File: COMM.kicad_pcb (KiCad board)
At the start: 4 copper layers, 90.2 x 95.9 mm, 41 parts, among them IC1 TLV61047DDCR, IC2 Voltage Converter (ADP7158ARD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, J1 SMA Conn. (RFPC-SMA30-F), U1 XBee Module (XBP9B-DMSTB002), U2 DMR Module (DMR818S-5W)

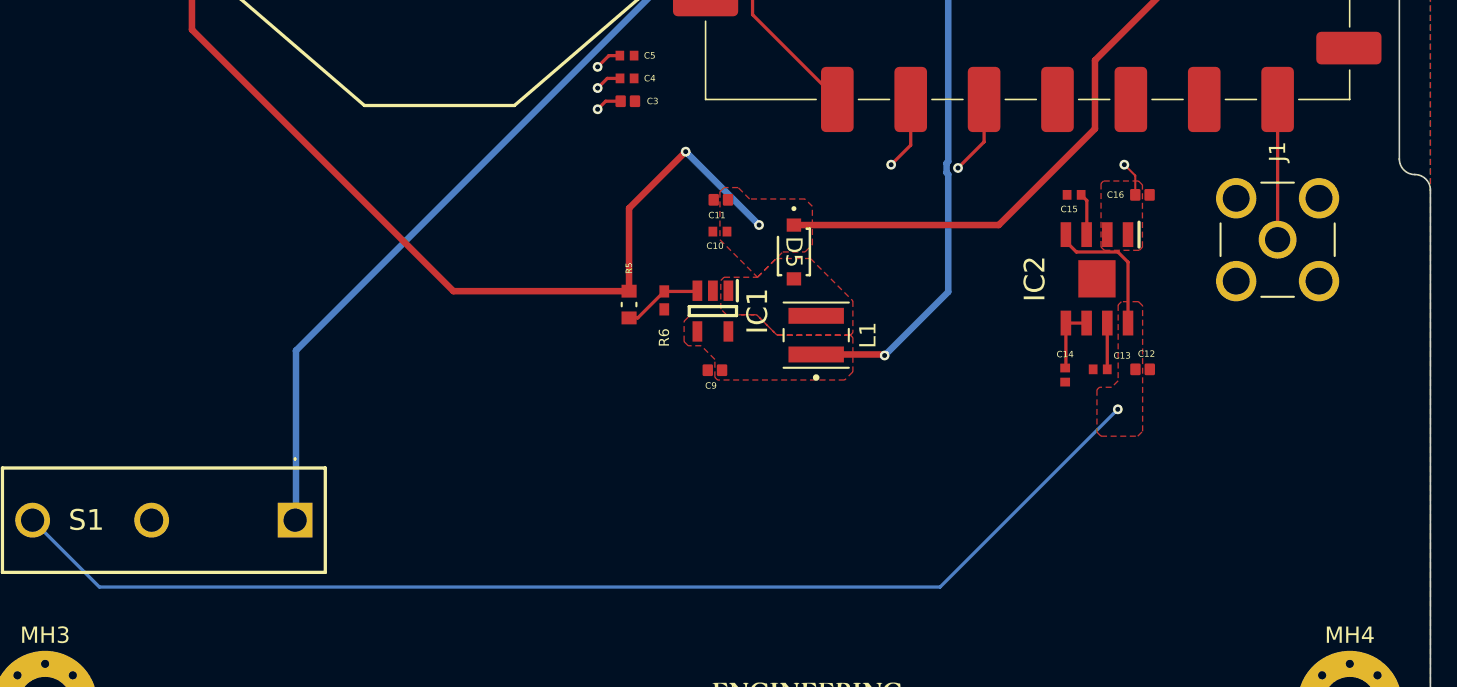
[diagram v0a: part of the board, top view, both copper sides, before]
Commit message: Switched positions for SMA connector and voltage regulator.
Signed-off-by: Logan Tolbert <xem6df@virginia.edu>
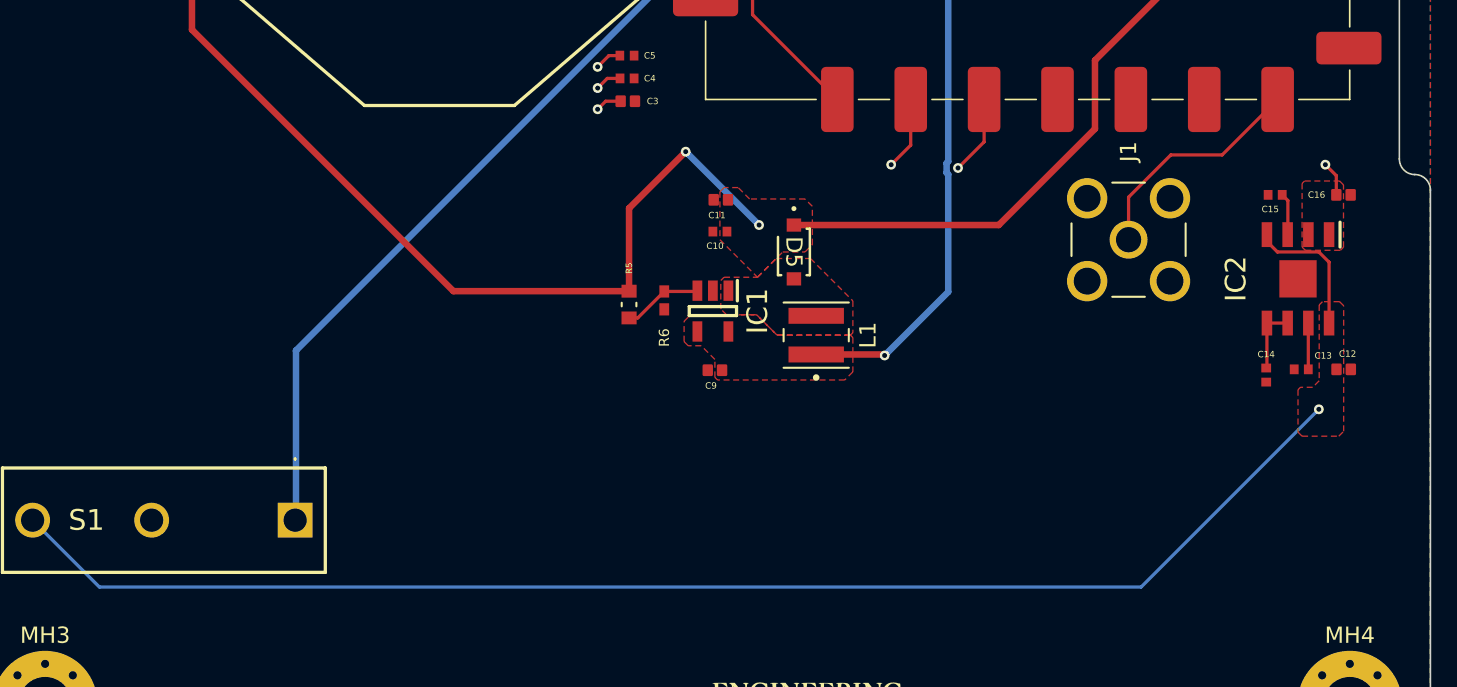
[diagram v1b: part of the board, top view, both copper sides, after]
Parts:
- moved C13 12.3 mm to (183.8, 123.3)
- moved C15 12.3 mm to (182.2, 112.7)
- moved IC2 12.3 mm to (183.7, 117.8)
- moved C12 12.3 mm to (186.4, 123.3)
- moved C14 12.3 mm to (181.7, 123.7)
- moved C16 12.3 mm to (186.4, 112.7)
- moved J1 9.14 mm to (173.3, 115.4)
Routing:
- net /Voltage Converter/VIN: track 81.3 -> 93.6 mm
- net /DMR818S 5W RF Module/ANT: track 8.60 -> 14.2 mm
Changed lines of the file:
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@@
 		(placed yes)
 		(layer "F.Cu")
-		(at 169.371 123.7 -90)
+		(at 181.7 123.7 -90)
 		(property "Reference" "C14"
 			(at -1.27 0 0)
@@
 	(footprint "RFPC-SMA30-F:GRADCONN_RFPC-SMA30-F"
 		(layer "F.Cu")
-		(at 182.4 115.4)
+		(at 173.26 115.4)
 		(property "Reference" "J1"
 			(at 0 -5.4 90)
@@
 		(placed yes)
 		(layer "F.Cu")
-		(at 171.321 117.8 -90)
+		(at 183.65 117.8 -90)
 		(descr "SOIC_N_EP")
 		(tags "Integrated Circuit")
@@
 	(footprint "C_10uF:CAPC1005X70N"
 		(layer "F.Cu")
-		(at 174.121 123.35)
+		(at 186.45 123.35)
 		(property "Reference" "C12"
 			(at 0.24 -0.95 0)
@@
 		(placed yes)
 		(layer "F.Cu")
-		(at 169.921 112.65 180)
+		(at 182.25 112.65 180)
 		(property "Reference" "C15"
 			(at 0.3 -0.88 0)
@@
 		(placed yes)
 		(layer "F.Cu")
-		(at 171.521 123.35 180)
+		(at 183.85 123.35 180)
 		(property "Reference" "C13"
 			(at -1.3462 0.8382 0)
@@
 		(placed yes)
 		(layer "F.Cu")
-		(at 174.11 112.65)
+		(at 186.439 112.65)
 		(property "Reference" "C16"
 			(at -1.651 0 0)
@@
 	)
 	(segment
-		(start 170.353 112.65)
-		(end 170.7 112.997)
+		(start 182.682 112.65)
+		(end 183.029 112.997)
 		(width 0.2)
 		(layer "F.Cu")
@@
 	)
 	(segment
-		(start 170.7 112.997)
-		(end 170.7 115.074)
+		(start 183.029 112.997)
+		(end 183.029 115.074)
 		(width 0.2)
 		(layer "F.Cu")
@@
 	)
 	(segment
-		(start 170.7 115.074)
-		(end 170.686 115.088)
+		(start 183.029 115.074)
+		(end 183.015 115.088)
 		(width 0.2)
 		(layer "F.Cu")
@@
 	)
 	(segment
-		(start 169.416 123.223)
-		(end 169.371 123.268)
+		(start 181.745 123.223)
+		(end 181.7 123.268)
 		(width 0.2)
 		(layer "F.Cu")
@@
 	)
 	(segment
-		(start 169.416 120.512)
-		(end 170.686 120.512)
+		(start 181.745 120.512)
+		(end 183.015 120.512)
 		(width 0.2)
 		(layer "F.Cu")
@@
 	)
 	(segment
-		(start 169.416 120.512)
-		(end 169.416 123.223)
+		(start 181.745 120.512)
+		(end 181.745 123.223)
 		(width 0.2)
 		(layer "F.Cu")
@@
 	)
 	(segment
-		(start 171.953 123.35)
-		(end 171.953 120.515)
+		(start 184.282 123.35)
+		(end 184.282 120.515)
 		(width 0.2)
 		(layer "F.Cu")
@@
 	)
 	(segment
-		(start 171.953 120.515)
-		(end 171.956 120.512)
+		(start 184.282 120.515)
+		(end 184.285 120.512)
 		(width 0.2)
 		(layer "F.Cu")
@@
 	)
 	(segment
-		(start 173.671 112.65)
-		(end 173.671 111.471)
-		(width 0.127)
+		(start 186 112.65)
+		(end 186 111.471)
+		(width 0.2)
 		(layer "F.Cu")
 		(net 9)
@@
 	)
 	(segment
-		(start 173.671 111.471)
-		(end 173 110.8)
-		(width 0.127)
+		(start 186 111.471)
+		(end 185.329 110.8)
+		(width 0.2)
 		(layer "F.Cu")
 		(net 9)
@@
 	)
 	(via
-		(at 173 110.8)
+		(at 185.329 110.8)
 		(size 0.6)
 		(drill 0.3)
@@
 	)
 	(segment
-		(start 182.4 106.8)
-		(end 182.4 115.4)
+		(start 173.26 112.792056)
+		(end 175.852056 110.2)
+		(width 0.2)
+		(layer "F.Cu")
+		(net 16)
+	)
+	(segment
+		(start 179 110.2)
+		(end 182.4 106.8)
+		(width 0.2)
+		(layer "F.Cu")
+		(net 16)
+	)
+	(segment
+		(start 175.852056 110.2)
+		(end 179 110.2)
+		(width 0.2)
+		(layer "F.Cu")
+		(net 16)
+	)
+	(segment
+		(start 173.26 115.4)
+		(end 173.26 112.792056)
 		(width 0.2)
 		(layer "F.Cu")
@@
 	)
 	(segment
-		(start 170.06 116.152)
-		(end 169.416 115.508)
+		(start 182.389 116.152)
+		(end 181.745 115.508)
 		(width 0.2)
 		(layer "F.Cu")
@@
 	)
 	(segment
-		(start 173.226 116.778)
-		(end 172.6 116.152)
+		(start 185.555 116.778)
+		(end 184.929 116.152)
 		(width 0.2)
 		(layer "F.Cu")
@@
 	)
 	(segment
-		(start 172.6 116.152)
-		(end 170.06 116.152)
+		(start 184.929 116.152)
+		(end 182.389 116.152)
 		(width 0.2)
 		(layer "F.Cu")
@@
 	)
 	(segment
-		(start 169.416 115.508)
-		(end 169.416 115.088)
+		(start 181.745 115.508)
+		(end 181.745 115.088)
 		(width 0.2)
 		(layer "F.Cu")
@@
 	)
 	(segment
-		(start 173.226 120.512)
-		(end 173.226 116.778)
+		(start 185.555 120.512)
+		(end 185.555 116.778)
 		(width 0.2)
 		(layer "F.Cu")
@@
 	)
 	(via
-		(at 172.6 125.8)
+		(at 184.929 125.8)
 		(size 0.6)
 		(drill 0.3)
@@
 	)
 	(segment
-		(start 106.05 132.6)
-		(end 110.15 136.7)
+		(start 110.15 136.7)
+		(end 174.029 136.7)
 		(width 0.2)
 		(layer "B.Cu")
@@
 	)
 	(segment
-		(start 161.7 136.7)
-		(end 172.6 125.8)
+		(start 174.029 136.7)
+		(end 184.929 125.8)
 		(width 0.2)
 		(layer "B.Cu")
@@
 	)
 	(segment
-		(start 110.15 136.7)
-		(end 161.7 136.7)
+		(start 106.05 132.6)
+		(end 110.15 136.7)
 		(width 0.2)
 		(layer "B.Cu")
@@
 		(polygon
 			(pts
-				(xy 174.109983 112.039) (xy 173.870983 111.8) (xy 171.720983 111.8) (xy 171.570983 111.95) (xy 171.570983 115.85)
-				(xy 171.770983 116.05) (xy 173.920983 116.05) (xy 174.109983 115.861)
+				(xy 186.438983 112.039) (xy 186.199983 111.8) (xy 184.049983 111.8) (xy 183.899983 111.95) (xy 183.899983 115.85)
+				(xy 184.099983 116.05) (xy 186.249983 116.05) (xy 186.438983 115.861)
 			)
 		)
@@
 		(polygon
 			(pts
-				(xy 174.120983 119.45) (xy 173.870983 119.2) (xy 172.820983 119.2) (xy 172.620983 119.4) (xy 172.620983 124.05)
-				(xy 172.220983 124.45) (xy 171.470983 124.45) (xy 171.320983 124.6) (xy 171.320983 127.2) (xy 171.570983 127.45)
-				(xy 173.820983 127.45) (xy 174.120983 127.15)
+				(xy 186.449983 119.45) (xy 186.199983 119.2) (xy 185.149983 119.2) (xy 184.949983 119.4) (xy 184.949983 124.05)
+				(xy 184.549983 124.45) (xy 183.799983 124.45) (xy 183.649983 124.6) (xy 183.649983 127.2) (xy 183.899983 127.45)
+				(xy 186.149983 127.45) (xy 186.449983 127.15)
 			)
 		)
@@
 		)
 	)
+	(group ""
+		(members "6bd41f40-2926-4697-b4bb-54f9e0ba9d41" "8675ddac-3444-43b7-9ae6-c6384b4b4ff4"
+			"bca501b6-a9c0-43b3-8d7a-0dfeb5b05f0d" "eecb56da-566d-4d54-92f7-bcf80e9436b0"
+		)
+	)
